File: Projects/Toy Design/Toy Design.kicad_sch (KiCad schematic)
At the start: 39 parts, among them J1 Conn_01x01_Pin, J2 Conn_01x01_Pin, U1 TLV61048DBVR, U10 STM32G030K6T6, U11 MCP3208-CI/SL, U2 MCP73123, U3 NCP1117-5.0_SOT223, U4 MLX90333, U5 A1330, U6 A1330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

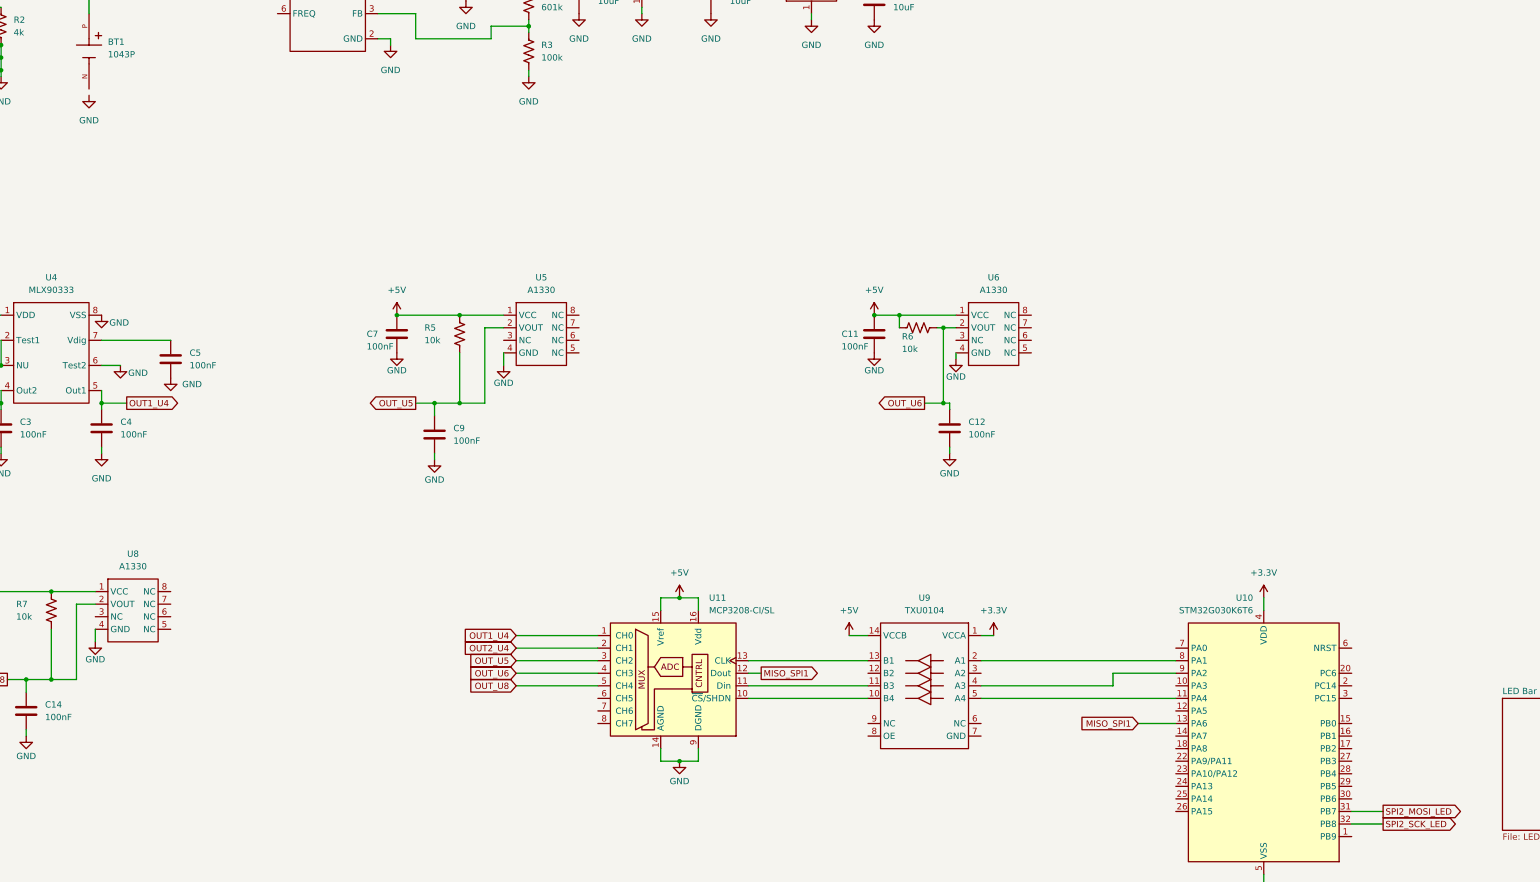
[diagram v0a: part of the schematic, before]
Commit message: started pcb post led bar
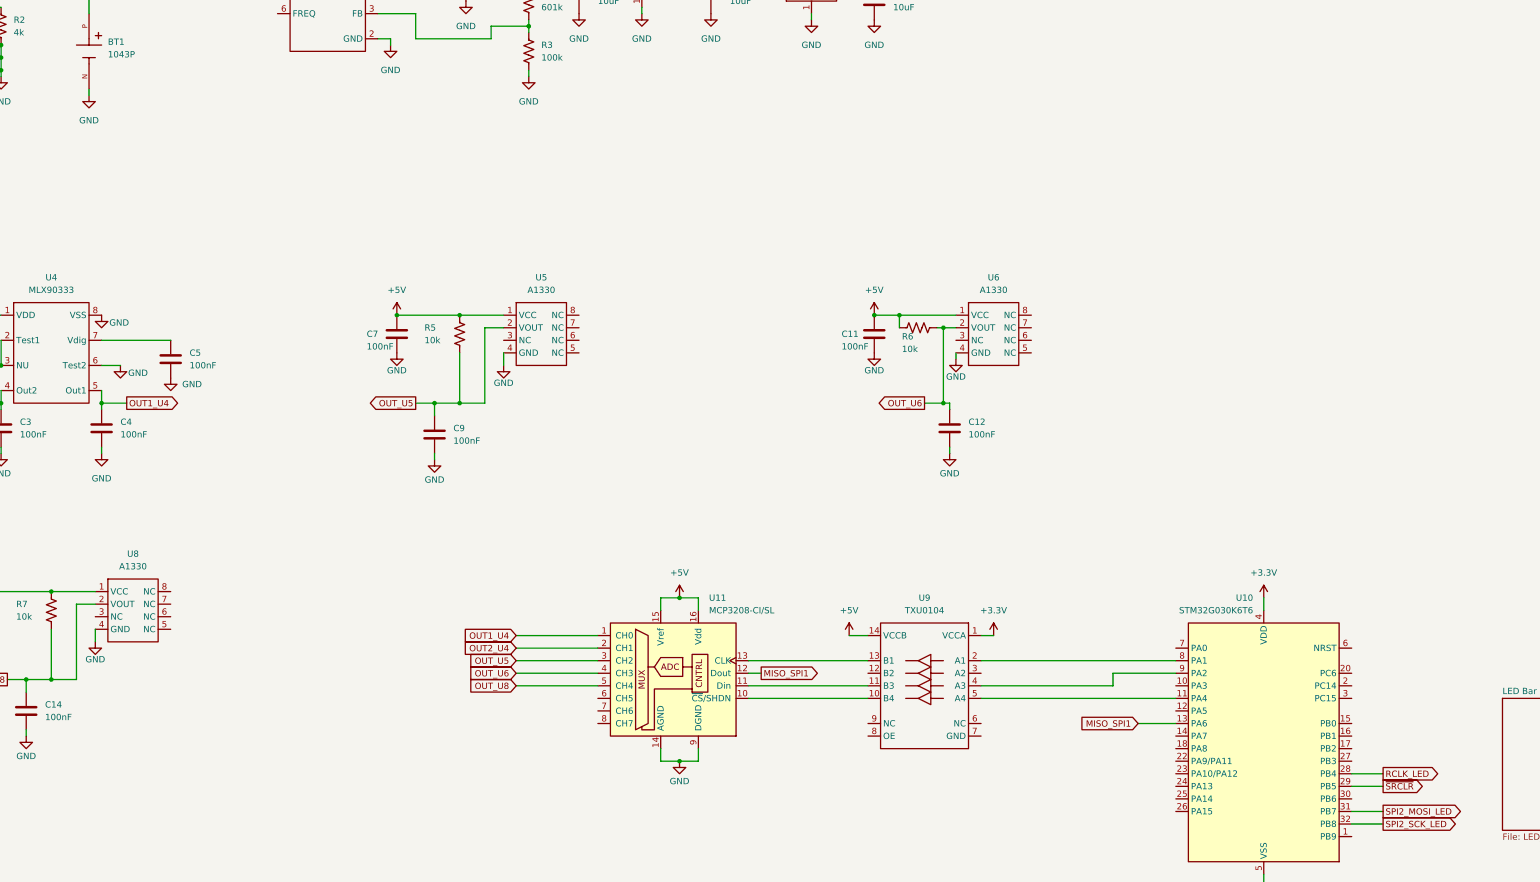
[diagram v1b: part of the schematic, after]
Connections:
- net GND: now also BT1.N
- net RCLK_LED: now reaches U10.28 (PB4)
- net ~{SRCLR}: now reaches U10.29 (PB5)
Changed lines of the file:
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@@
+	(wire
+		(pts
+			(xy 334.01 200.66) (xy 340.36 200.66)
+		)
+		(stroke
+			(width 0)
+			(type default)
+		)
+	)
 	(wire
 		(pts
@@
 	(wire
 		(pts
+			(xy 334.01 203.2) (xy 340.36 203.2)
+		)
+		(stroke
+			(width 0)
+			(type default)
+		)
+	)
+	(wire
+		(pts
 			(xy 60.96 135.89) (xy 60.96 134.62)
 		)
@@
 		(pts
 			(xy 177.8 39.37) (xy 177.8 38.1)
+		)
+		(stroke
+			(width 0)
+			(type default)
+		)
+	)
+	(wire
+		(pts
+			(xy 78.74 62.23) (xy 78.74 63.5)
 		)
 		(stroke
@@
 		)
 	)
+	(global_label "RCLK_LED"
+		(shape output)
+		(at 340.36 200.66 0)
+		(fields_autoplaced yes)
+		(effects
+			(font
+				(size 1.27 1.27)
+			)
+			(justify left)
+		)
+		(property "Intersheetrefs" "${INTERSHEET_REFS}"
+			(at 352.598 200.66 0)
+			(hide yes)
+			(show_name no)
+			(do_not_autoplace no)
+			(effects
+				(font
+					(size 1.27 1.27)
+				)
+				(justify left)
+			)
+		)
+	)
 	(global_label "OUT1_U4"
 		(shape output)
@@
 			)
 		)
+	)
+	(global_label "~{SRCLR}"
+		(shape output)
+		(at 340.36 203.2 0)
+		(fields_autoplaced yes)
+		(effects
+			(font
+				(size 1.27 1.27)
+			)
+			(justify left)
+		)
+		(property "Intersheetrefs" "${INTERSHEET_REFS}"
+			(at 349.3928 203.2 0)
+			(hide yes)
+			(show_name no)
+			(do_not_autoplace no)
+			(effects
+				(font
+					(size 1.27 1.27)
+				)
+				(justify left)
+			)
+		)

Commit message: updated sonme stuff
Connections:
- net +5V: now also U9.8 (OE)
- net GND: now also U9.7 (GND)
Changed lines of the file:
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@@
 	(wire
 		(pts
+			(xy 260.35 194.31) (xy 260.35 193.04)
+		)
+		(stroke
+			(width 0)
+			(type default)
+		)
+	)
+	(wire
+		(pts
 			(xy 251.46 125.73) (xy 252.73 125.73)
 		)
@@
 	(wire
 		(pts
+			(xy 260.35 193.04) (xy 259.08 193.04)
+		)
+		(stroke
+			(width 0)
+			(type default)
+		)
+	)
+	(wire
+		(pts
 			(xy 140.97 36.83) (xy 143.51 36.83)
 		)
@@
 	(wire
 		(pts
+			(xy 232.41 193.04) (xy 236.22 193.04)
+		)
+		(stroke
+			(width 0)
+			(type default)
+		)
+	)
+	(wire
+		(pts
 			(xy 194.31 165.1) (xy 198.12 165.1)
 		)
@@
 	)
 	(symbol
+		(lib_id "power:+5V")
+		(at 232.41 193.04 0)
+		(unit 1)
+		(body_style 1)
+		(exclude_from_sim no)
+		(in_bom yes)
+		(on_board yes)
+		(in_pos_files yes)
+		(dnp no)
+		(fields_autoplaced yes)
+		(property "Reference" "#PWR057"
+			(at 232.41 196.85 0)
+			(hide yes)
+			(show_name no)
+			(do_not_autoplace no)
+			(effects
+				(font
+					(size 1.27 1.27)
+				)
+			)
+		)
+		(property "Value" "+5V"
+			(at 232.41 187.96 0)
+			(show_name no)
+			(do_not_autoplace no)
+			(effects
+				(font
+					(size 1.27 1.27)
+				)
+			)
+		)
+		(property "Footprint" ""
+			(at 232.41 193.04 0)
+			(hide yes)
+			(show_name no)
+			(do_not_autoplace no)
+			(effects
+				(font
+					(size 1.27 1.27)
+				)
+			)
+		)
+		(property "Datasheet" ""
+			(at 232.41 193.04 0)
+			(hide yes)
+			(show_name no)
+			(do_not_autoplace no)
+			(effects
+				(font
+					(size 1.27 1.27)
+				)
+			)
+		)
+		(property "Description" "Power symbol creates a global label with name \"+5V\""
+			(at 232.41 193.04 0)
+			(hide yes)
+			(show_name no)
+			(do_not_autoplace no)
+			(effects
+				(font
+					(size 1.27 1.27)
+				)
+			)
+		)
+		(pin "1"
+		)
+		(instances
+			(project "Toy Design"
+				(path "/c85456d0-c9f8-47a9-8124-8a5f769becea"
+					(reference "#PWR057")
+					(unit 1)
+				)
+			)
+		)
+	)
+	(symbol
 		(lib_id "Device:C")
 		(at 204.47 43.18 0)
@@
 					(unit 1)
 				)
+			)
+		)
+	)
+	(symbol
+		(lib_id "power:GND")
+		(at 260.35 194.31 0)
+		(unit 1)
+		(body_style 1)
+		(exclude_from_sim no)
+		(in_bom yes)
+		(on_board yes)
+		(in_pos_files yes)
+		(dnp no)
+		(property "Reference" "#PWR056"
+			(at 260.35 200.66 0)
+			(hide yes)
+			(show_name no)
+			(do_not_autoplace no)
+			(effects
+				(font
+					(size 1.27 1.27)
+				)
+			)
+		)
+		(property "Value" "GND"
+			(at 260.35 198.374 0)
+			(show_name no)
+			(do_not_autoplace no)
+			(effects
+				(font
+					(size 1.27 1.27)
+				)
+			)
+		)
+		(property "Footprint" ""
+			(at 260.35 194.31 0)
+			(hide yes)
+			(show_name no)
+			(do_not_autoplace no)
+			(effects
+				(font
+					(size 1.27 1.27)
+				)
+			)
+		)
+		(property "Datasheet" ""
+			(at 260.35 194.31 0)
+			(hide yes)
+			(show_name no)
+			(do_not_autoplace no)
+			(effects
+				(font
+					(size 1.27 1.27)
+				)
+			)
+		)
+		(property "Description" "Power symbol creates a global label with name \"GND\" , ground"
+			(at 260.35 194.31 0)
+			(hide yes)
+			(show_name no)
+			(do_not_autoplace no)
+			(effects
+				(font
+					(size 1.27 1.27)
+				)
+			)
+		)
+		(pin "1"
+		)
+		(instances
+			(project "Toy Design"
+				(path "/c85456d0-c9f8-47a9-8124-8a5f769becea"
+					(reference "#PWR056")
+					(unit 1)
+				)

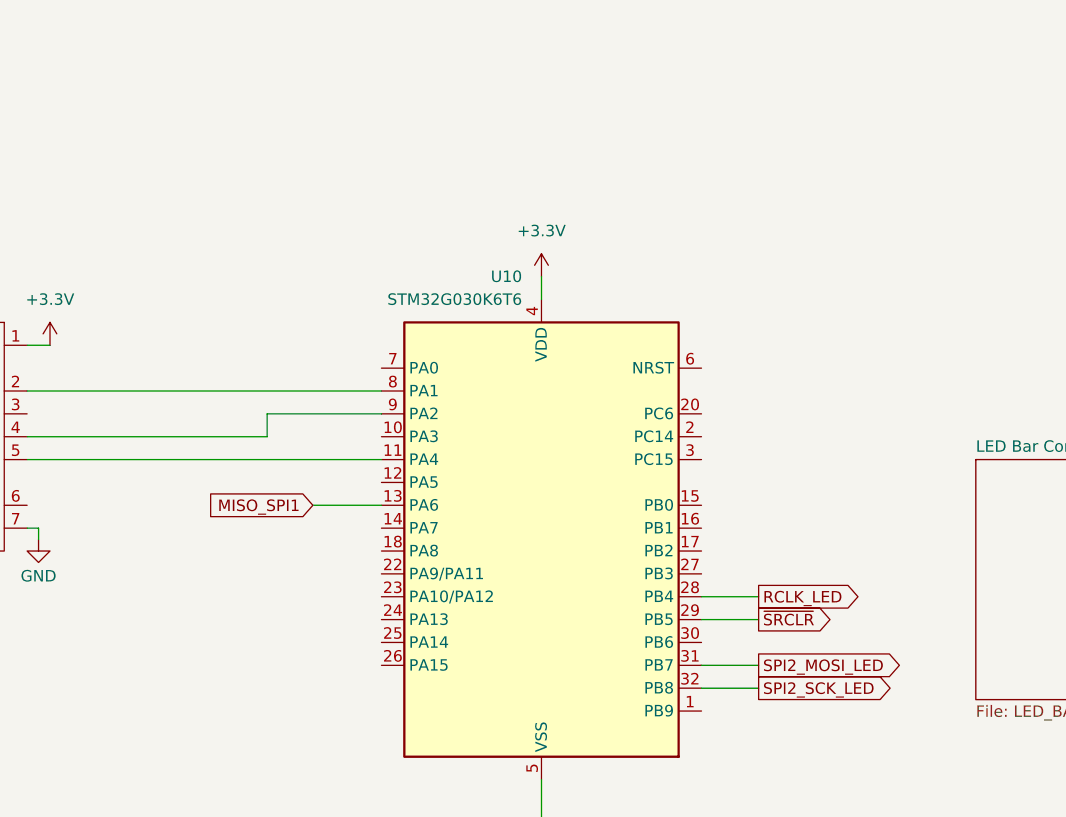
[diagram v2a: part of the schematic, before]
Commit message: Updating with programmer nets but no connector YET
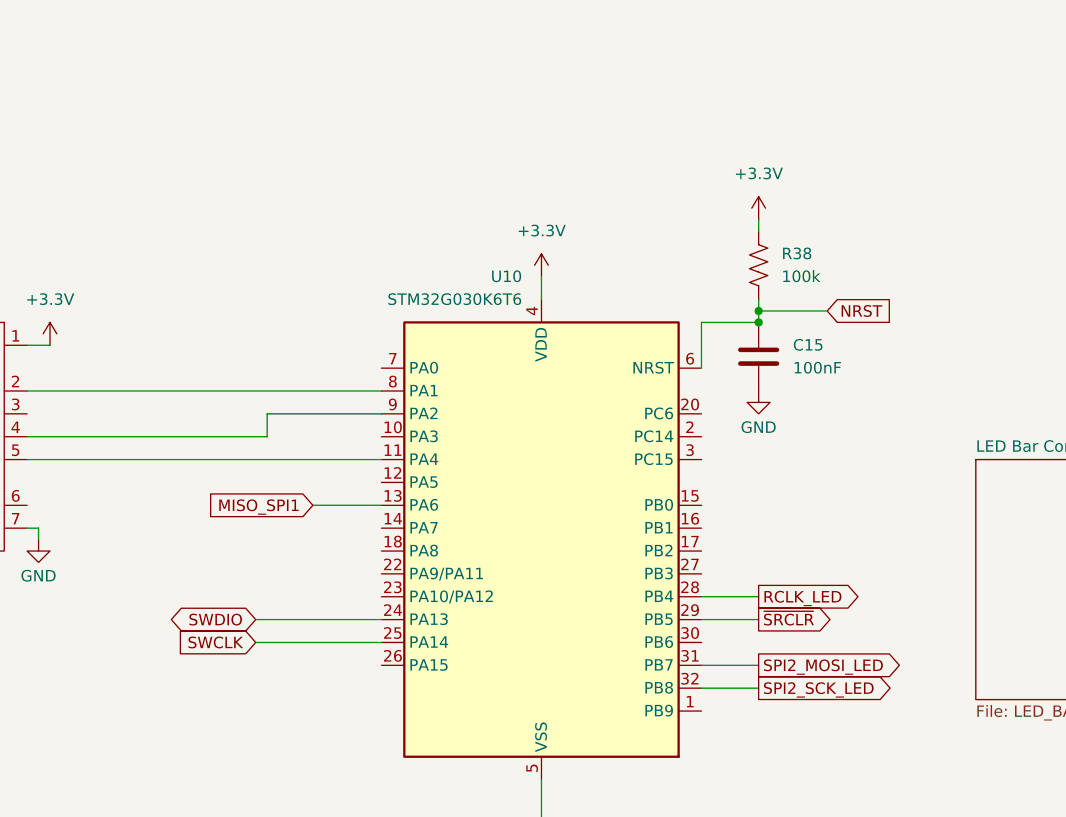
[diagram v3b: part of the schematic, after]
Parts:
- added C15: 100nF, Capacitor_SMD:C_0805_2012Metric_Pad1.18x1.45mm_HandSolder, symbol Toy_Design:C
- added R38: 100k, Resistor_SMD:R_0805_2012Metric_Pad1.20x1.40mm_HandSolder, symbol Device:R_US
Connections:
- net +3.3V: now also R38.1
- net GND: now also C15.2
- net SWDIO: now reaches U10.24 (PA13)
- net SWCLK: now reaches U10.25 (PA14)
- net NRST: now reaches U10.6 (NRST)
- net NRST: now also C15.1, R38.2
